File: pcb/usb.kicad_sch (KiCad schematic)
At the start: 42 parts, among them J6 USB4105-GF-A, J7 S2B-PH-SM4-TB, Q1 DMP3099L-7, Q2 DMG3418L, Q3 DMG3418L, SW1 400MSP1R6BLKM6QE, U151 AP2112K-3.3, U152 BQ29700DSER, U153 MCP73831T-2ACI/OT, U154 APX803L05-35SA-7

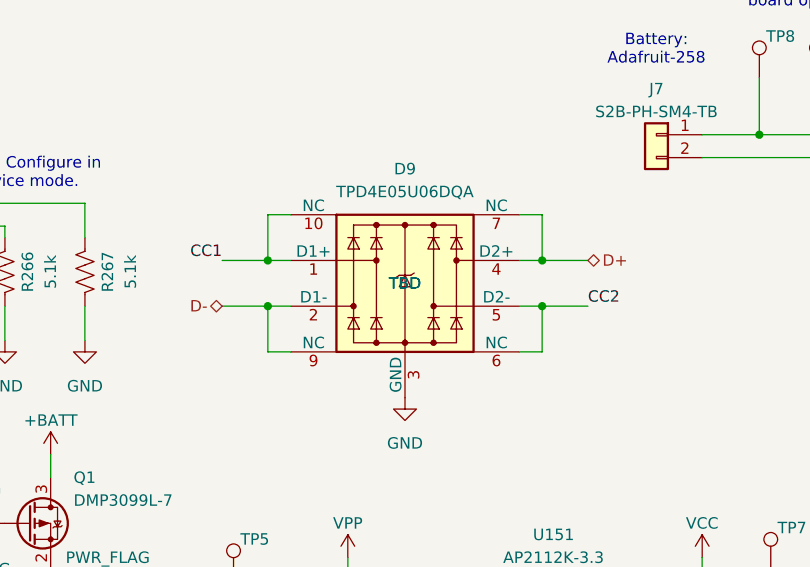
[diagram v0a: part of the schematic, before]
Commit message: BOM completed
- OEPSPN & MPN fully complete
- .csv BOM file updated
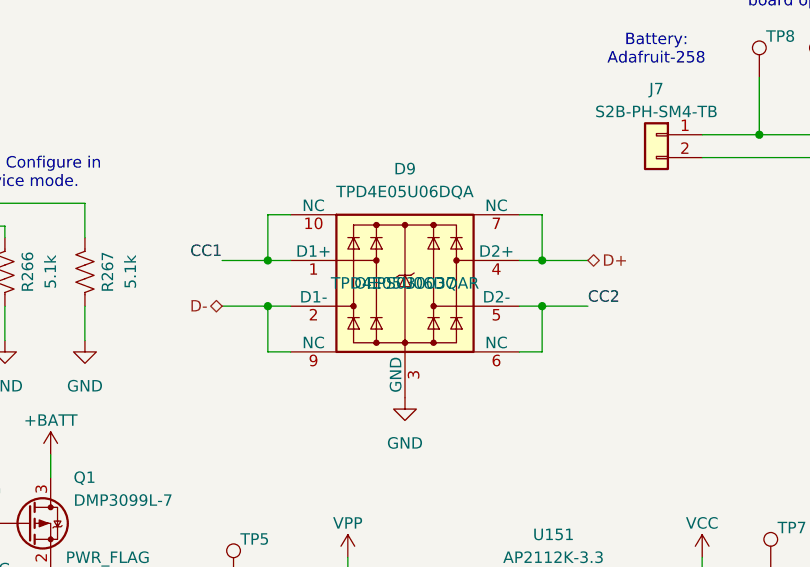
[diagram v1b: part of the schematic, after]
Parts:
- D9: MPN TBD -> TPD4E05U06DQAR; OEPSPN TBD -> OEPS030037
- R263: MPN CRCW040210K0FKED -> ERJ-2RKF4702X; OEPSPN OEPS020030 -> OEPS020017
- U154: MPN TBD -> APX803L05-35SA-7; OEPSPN TBD -> OEPS080168
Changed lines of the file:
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@@
 			)
 		)
-		(property "MPN" "TBD"
+		(property "MPN" "APX803L05-35SA-7"
 			(at 142.24 143.51 0)
 			(effects
@@
 			)
 		)
-		(property "OEPSPN" "TBD"
+		(property "OEPSPN" "OEPS080168"
 			(at 142.24 143.51 0)
 			(effects
@@
 			)
 		)
-		(property "MPN" "TBD"
+		(property "MPN" "TPD4E05U06DQAR"
 			(at 124.46 58.42 0)
 			(effects
@@
 			)
 		)
-		(property "OEPSPN" "TBD"
+		(property "OEPSPN" "OEPS030037"
 			(at 124.46 58.42 0)
 			(effects
@@
 			)
 		)
-		(property "MPN" "CRCW040210K0FKED"
+		(property "MPN" "ERJ-2RKF4702X"
 			(at 97.79 134.62 0)
 			(effects
@@
 			)
 		)
-		(property "OEPSPN" "OEPS020030"
+		(property "OEPSPN" "OEPS020017"
 			(at 97.79 134.62 0)
 			(effects

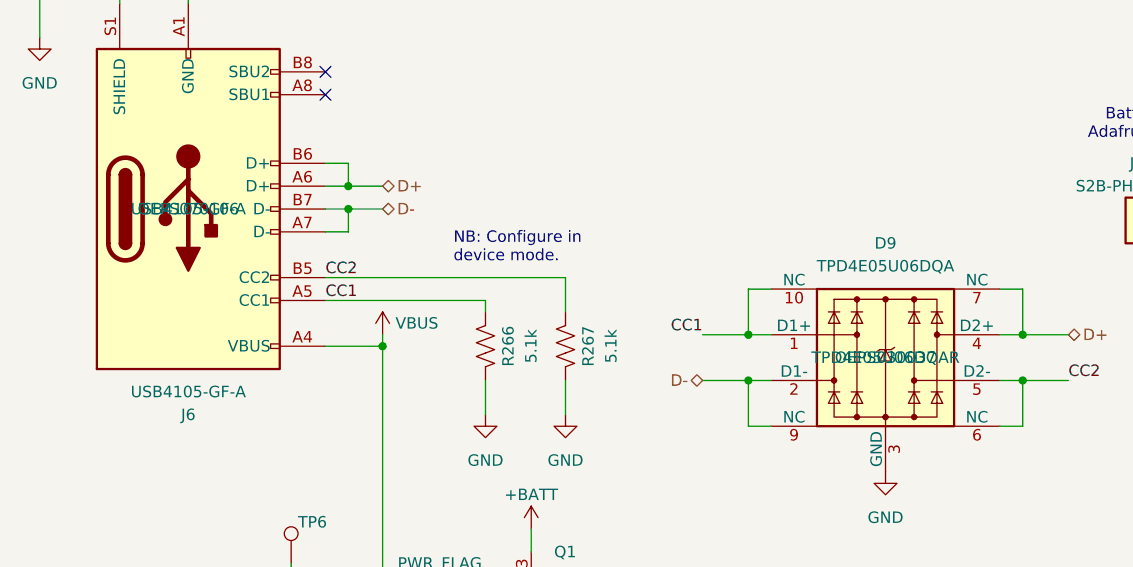
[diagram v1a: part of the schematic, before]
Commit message: OEPSPN corrected
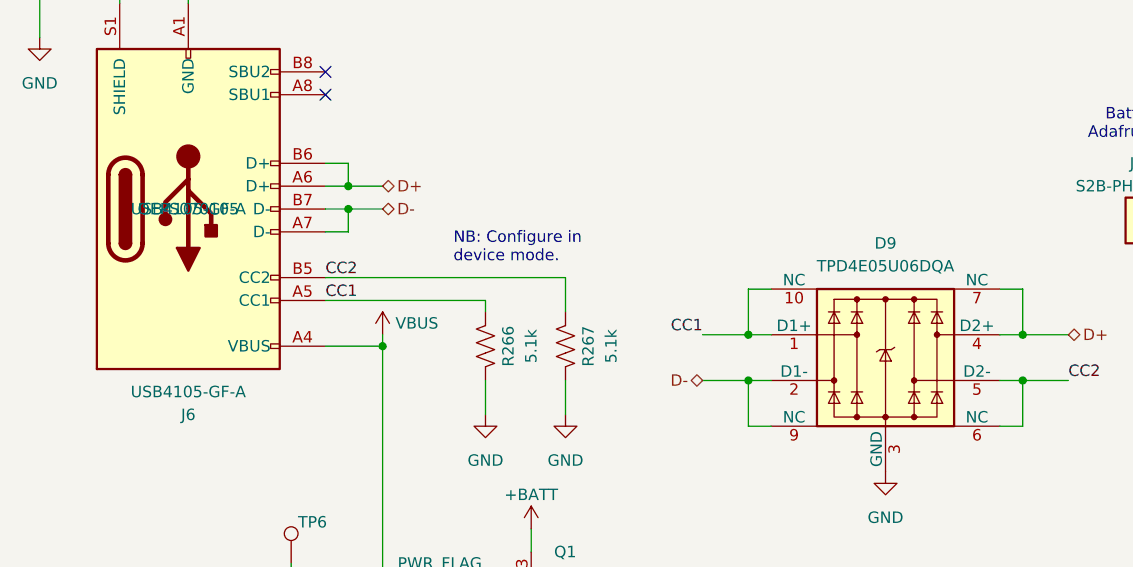
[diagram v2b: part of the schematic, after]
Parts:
- J6: OEPSPN OEPS070106 -> OEPS070105
- J7: OEPSPN OEPS070105 -> OEPS070106
- R270: OEPSPN OEPS020037 -> OEPS020139
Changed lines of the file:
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@@
 			)
 		)
-		(property "OEPSPN" "OEPS070106"
+		(property "OEPSPN" "OEPS070105"
 			(at 46.99 41.91 0)
 			(effects
@@
 			)
 		)
-		(property "OEPSPN" "OEPS020037"
+		(property "OEPSPN" "OEPS020139"
 			(at 182.88 60.96 0)
 			(effects
@@
 					(size 1.27 1.27)
 				)
+				(hide yes)
 			)
 		)
@@
 					(size 1.27 1.27)
 				)
+				(hide yes)
 			)
 		)
@@
 			)
 		)
-		(property "OEPSPN" "OEPS070105"
+		(property "OEPSPN" "OEPS070106"
 			(at 152.4 41.91 0)
 			(effects

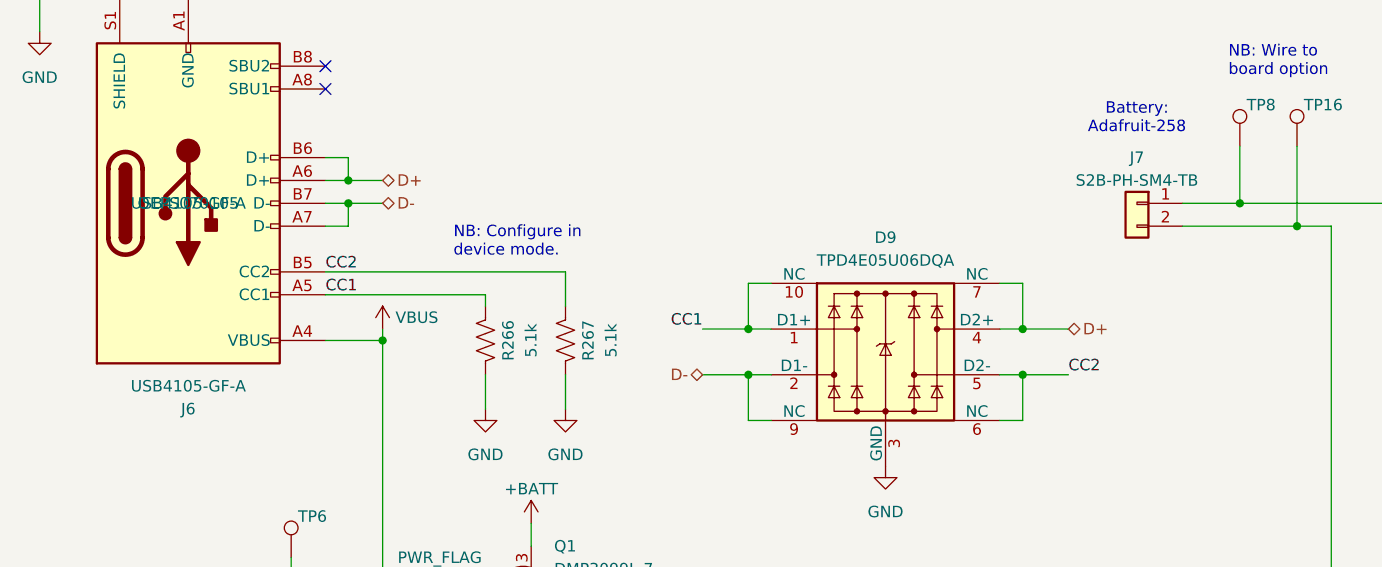
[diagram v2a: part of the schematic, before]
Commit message: .csv BOM updated with last changes
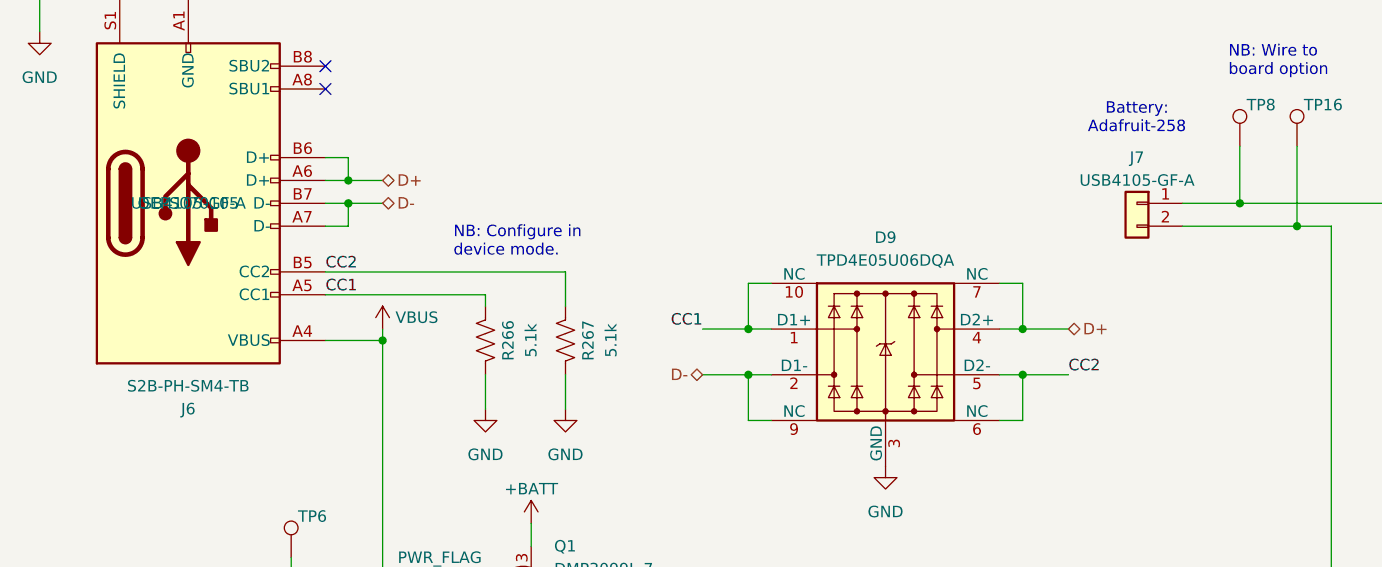
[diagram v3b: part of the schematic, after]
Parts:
- J6: value USB4105-GF-A -> S2B-PH-SM4-TB
- J7: value S2B-PH-SM4-TB -> USB4105-GF-A
- R270: MPN RC0402FR-07330RL -> CRCW0603330RFKEAC
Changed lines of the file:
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@@
 			)
 		)
-		(property "Value" "USB4105-GF-A"
+		(property "Value" "S2B-PH-SM4-TB"
 			(at 46.99 62.23 0)
 			(effects
@@
 			)
 		)
-		(property "MPN" "RC0402FR-07330RL"
+		(property "MPN" "CRCW0603330RFKEAC"
 			(at 182.88 60.96 0)
 			(effects
@@
 			)
 		)
-		(property "Value" "S2B-PH-SM4-TB"
+		(property "Value" "USB4105-GF-A"
 			(at 152.4 39.37 0)
 			(effects
